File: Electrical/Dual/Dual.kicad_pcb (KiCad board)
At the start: 2 copper layers, 140 x 70 mm, 190 parts, among them J101 01x04, J102 02x04, J103 01x04, J104 01x03, J105 01x03, J106 01x03, J107 01x03, J108 01x03, J109 01x03, J110 01x04, J111 01x04, J112 01x04, J113 01x04, J114 01x03, J115 01x03, J116 01x03, J117 01x03, J201 01x03, J202 01x04, J203 01x03, J204 01x04, J205 01x03, J206 USB_OTG, J207 01x04, J208 01x02, J209 01x04, J210 01x02, J211 01x02, J212 4PostTerm, J213 2PostTerm, J214 2PostTerm, J215 2PostTerm, J216 2PostTerm, J217 2PostTerm, J218 01x02, J219 01x02, Q201 FDC6420C, Q202 FDG1024NZ, Q301 FDC6420C, Q401 FDC6420C, U201 TPD4S012, U202 ACS712ELCTR-05B-T, U203 ACS712ELCTR-05B-T, U204 24LC256, U205 LM2576HVS-ADJ, U206 LM2576HVS-ADJ, x100 02x05, x101 RoutaCell, x102 RoutaCell, x103 RoutaCell, x104 RoutaCell, x105 RoutaCell, x106 RoutaCell, x107 RoutaCell, x108 RoutaCell, x109 RoutaCell, x110 RoutaCell, x111 RoutaCell, x112 RoutaCell, x113 RoutaCell, x114 RoutaCell, x115 RoutaCell, x116 RoutaCell, x117 RoutaCell, x118 RoutaCell, x119 RoutaCell, x120 RoutaCell, x121 RoutaCell, x122 RoutaCell, x123 RoutaCell, x124 RoutaCell, x125 RoutaCell, x126 RoutaCell, x127 RoutaCell, x128 RoutaCell, x129 RoutaCell, x130 RoutaCell, x131 RoutaCell, x132 RoutaCell, x133 RoutaCell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

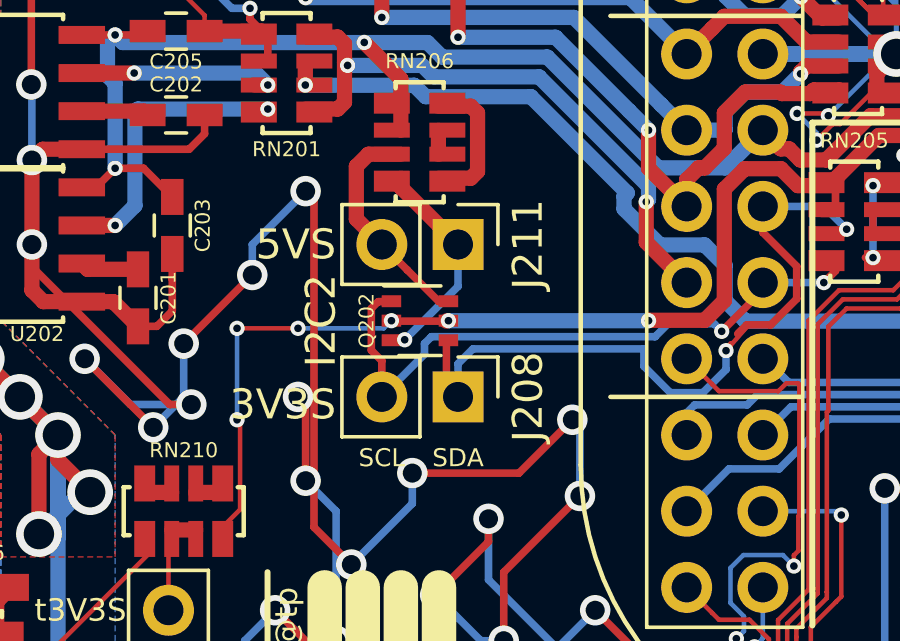
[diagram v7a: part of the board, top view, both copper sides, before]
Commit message: Made pin one consistantly SCL on both sets of I2C headers.
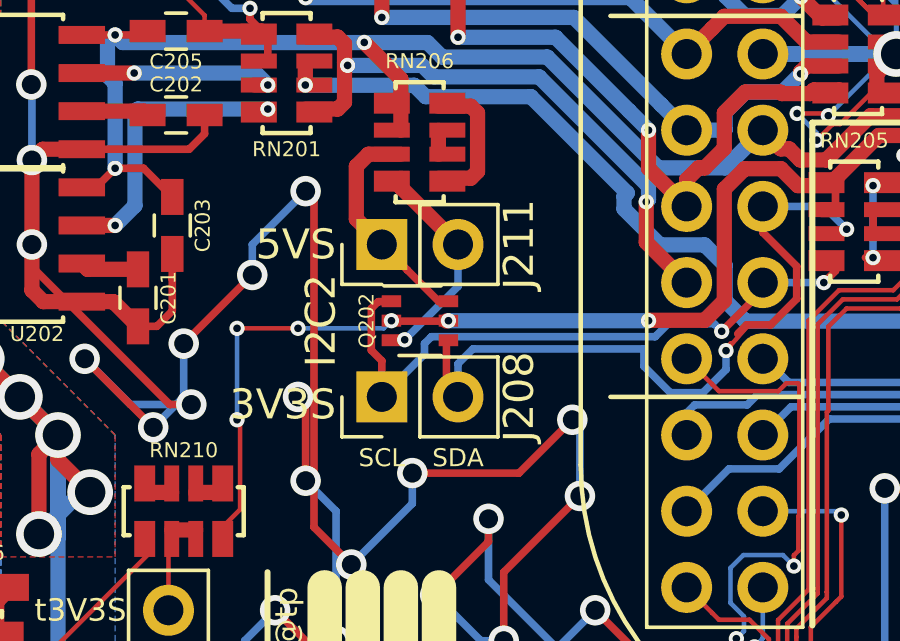
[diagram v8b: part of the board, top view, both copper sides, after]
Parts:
- moved J208 2.54 mm to (75.9, 107.6), turned to 90 degrees
- moved J211 2.54 mm to (75.9, 102.5), turned to 90 degrees
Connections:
- J208 pad 1: /Common/i2c2_sda -> /Common/i2c2_scl
- J208 pad 2: /Common/i2c2_scl -> /Common/i2c2_sda
- Q202 pad 3: Net-(J211-Pad1) -> Net-(J211-Pad2)
- Q202 pad 6: Net-(J211-Pad2) -> Net-(J211-Pad1)
- RN206 pad 3: Net-(J211-Pad2) -> Net-(J211-Pad1)
- RN206 pad 4: Net-(J211-Pad1) -> Net-(J211-Pad2)
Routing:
- net Net-(J211-Pad2): track 7.55 -> 7.43 mm, vias 0 -> 1
- net Net-(J211-Pad1): track 7.43 -> 7.55 mm, vias 1 -> 0
